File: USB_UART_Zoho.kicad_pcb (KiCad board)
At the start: 4 copper layers, 50 x 25 mm, 22 parts, among them J1 USB_C_Receptacle, J2 Peripherals, J4 VccIo_jumper, U1 FT232RL, U2 USBLC6-2P6

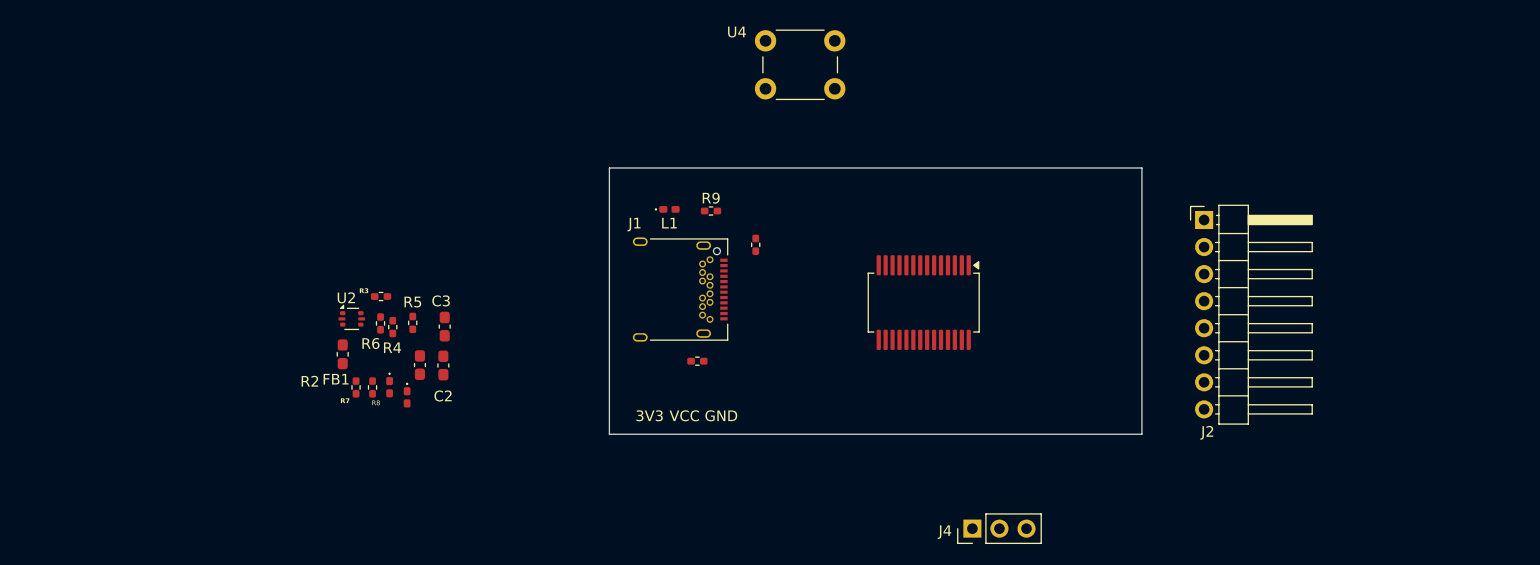
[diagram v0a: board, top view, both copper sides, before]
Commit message: USB type C changed to USB type A: some desgin changes in the routing
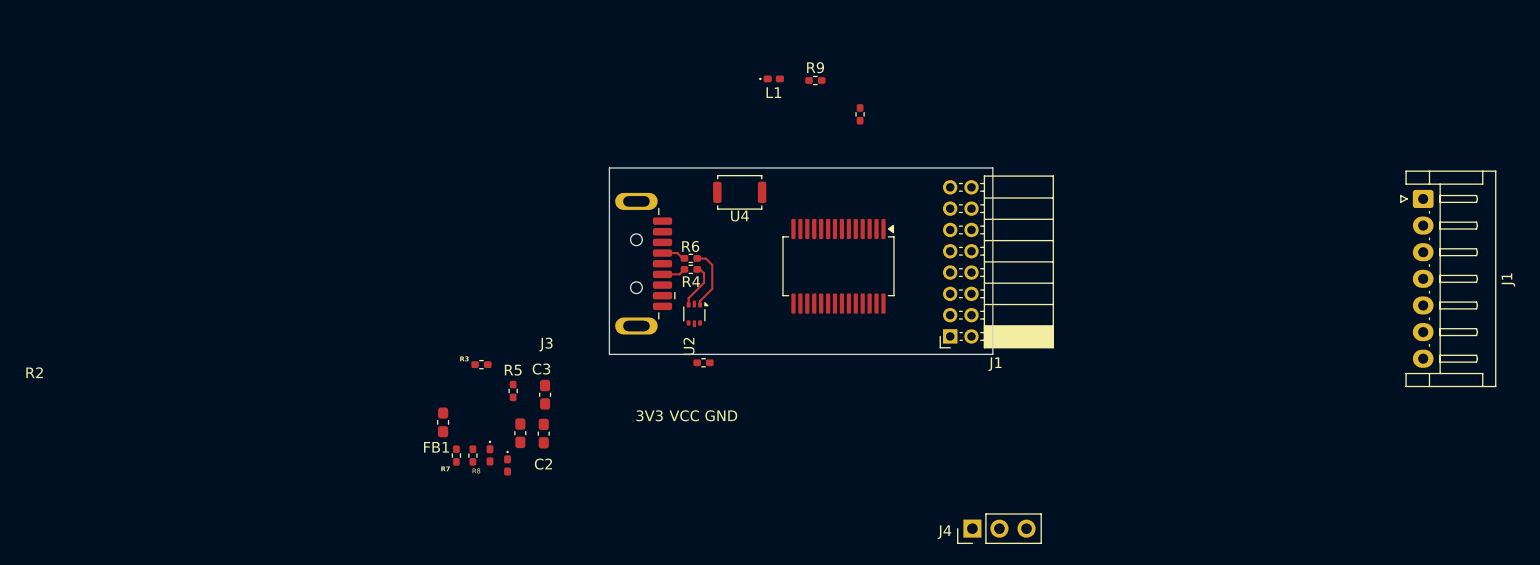
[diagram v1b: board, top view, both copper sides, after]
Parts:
- removed the J1 at (133.0, 95.0)
- removed J2: Peripherals, Connector_PinHeader_2.54mm:PinHeader_1x08_P2.54mm_Horizontal
- added J1: Conn_02x08_Counter_Clockwise, Connector_PinSocket_2.00mm:PinSocket_2x08_P2.00mm_Horizontal, F.Cu at (159.3, 99.4)
- added J1: Conn_01x07_Pin, Connector_JST:JST_EH_S7B-EH_1x07_P2.50mm_Horizontal, F.Cu at (203.7, 86.5)
- added J3: USB3_A, Connector_USB:USB3_A_Plug_Wuerth_692112030100_Horizontal, F.Cu at (121.4, 92.6)
- U4: footprint Button_Switch_THT:SW_PUSH_6mm_H5mm -> Button_Switch_SMD:SW_Push_SPST_NO_Alps_SKRK
- moved U2 32.2 mm to (135.2, 97.3), turned to -90 degrees
- moved R6 29.8 mm to (134.9, 92.1), turned to 180 degrees
- moved R4 28.5 mm to (134.9, 93.1), turned to 0 degrees
- moved R1 15.7 mm to (150.8, 78.6)
- moved L1 15.7 mm to (142.7, 75.2)
- moved R9 15.7 mm to (146.6, 75.4)
- moved U4 13.2 mm to (139.5, 85.9)
- moved C1 11.4 mm to (118.9, 108.5)
- moved FB1 11.4 mm to (111.7, 107.5)
- moved R7 11.4 mm to (112.9, 110.6)
- moved C3 11.4 mm to (121.2, 104.9)
- moved Rx_LED1 11.4 mm to (116.0, 110.6)
- moved Tx_LED1 11.4 mm to (117.7, 111.5)
- moved C2 11.4 mm to (121.1, 108.5)
- moved R3 11.4 mm to (115.2, 102.1)
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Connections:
- R6 pad 1: /D+ -> /d_P
- R6 pad 2: /d_P -> /D+
- U2 pad 1: /d_N -> /d_P
- U2 pad 3: /d_P -> /d_N
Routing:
- net /d_P: track 0.00 -> 5.88 mm
- net /d_N: track 0.00 -> 4.36 mm
- net /D+: track 0.00 -> 2.27 mm
- net /D-: track 0.00 -> 2.26 mm
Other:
- board size 50 x 25 mm -> 36 x 17.5 mm

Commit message: major rerouting done: decoupling capacitorsm and resistors placed
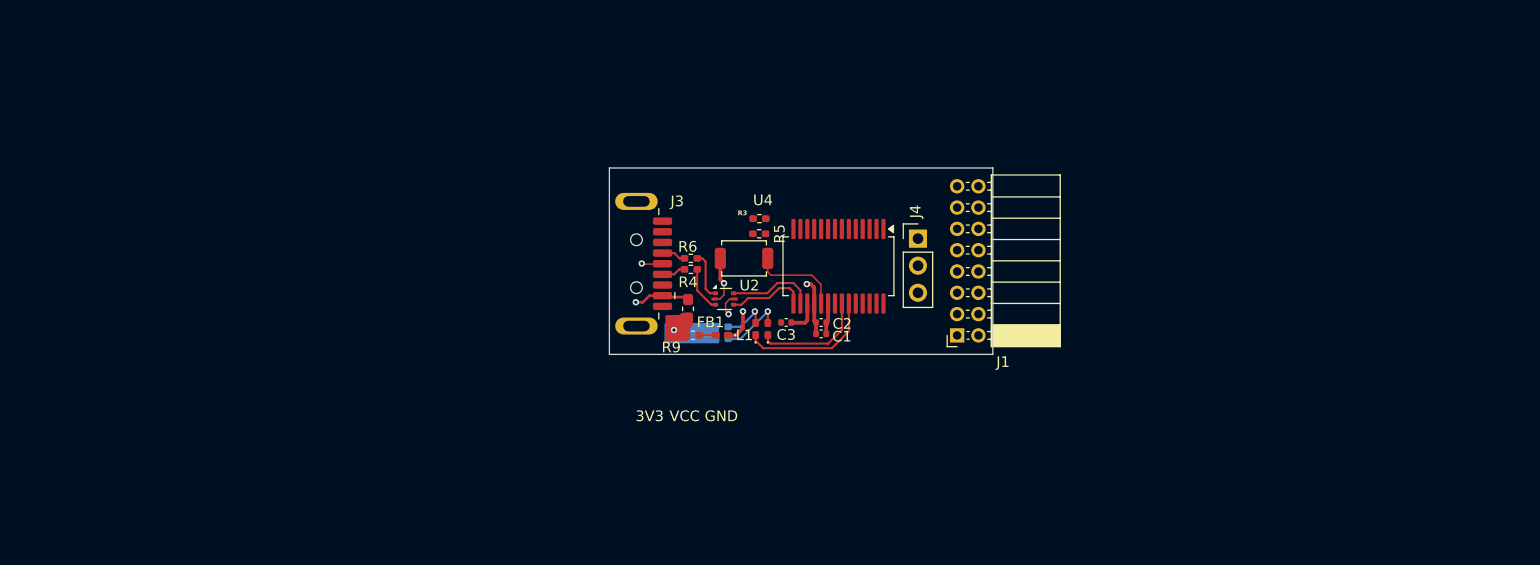
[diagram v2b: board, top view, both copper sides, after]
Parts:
- removed the J1 at (159.3, 99.4)
- removed the J1 at (203.7, 86.5)
- removed R1, R2: 5.1k, Resistor_SMD:R_0402_1005Metric_Pad0.72x0.64mm_HandSolder
- added J1: Conn_02x08_Counter_Clockwise, Connector_PinSocket_2.00mm:PinSocket_2x08_P2.00mm_Horizontal, F.Cu at (159.9, 99.3)
- C1, C2, C3: footprint Capacitor_SMD:C_0603_1608Metric_Pad1.08x0.95mm_HandSolder -> Capacitor_SMD:C_0402_1005Metric
- R7, R8: moved to B.Cu
- U4: footprint Button_Switch_SMD:SW_Push_SPST_NO_Alps_SKRK -> Button_Switch_SMD:SW_SPST_TS-1088-xR025
- moved C1 29.7 mm to (147.1, 99.2), turned to 180 degrees
- moved R3 29.5 mm to (141.4, 88.4)
- moved Rx_LED1 28.7 mm to (142.1, 98.7), turned to 90 degrees
- moved C2 28.1 mm to (147.1, 98.1), turned to 180 degrees
- moved J4 27.7 mm to (156.2, 90.2), turned to 0 degrees
- moved R7 27.7 mm to (137.8, 98.5), turned to 0 degrees
- moved R5 27.4 mm to (141.3, 89.8), turned to 0 degrees
- moved Tx_LED1 26.6 mm to (141.0, 98.7), turned to 90 degrees
- moved R9 26.5 mm to (135.1, 99.3), turned to 180 degrees
- moved R8 25.8 mm to (137.8, 99.6), turned to 0 degrees
- moved FB1 25.3 mm to (134.6, 96.8)
- moved L1 24.6 mm to (137.8, 99.3), turned to 180 degrees
- moved C3 23.6 mm to (143.9, 98.1), turned to 180 degrees
- moved U4 6.21 mm to (139.9, 92.1)
- moved U2 3.16 mm to (138.1, 95.9), turned to 0 degrees
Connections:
- FB1 pad 1: Net-(F1-Pad2) -> VBUS
- U1 pad 1: unconnected-(U1-TXD-Pad1) -> Net-(J1-Pin_1)
- U1 pad 10: unconnected-(U1-DCD-Pad10) -> Net-(J1-Pin_7)
- U1 pad 11: unconnected-(U1-CTS-Pad11) -> Net-(J1-Pin_4)
- U1 pad 2: unconnected-(U1-DTR-Pad2) -> Net-(J1-Pin_5)
- U1 pad 3: unconnected-(U1-RTS-Pad3) -> Net-(J1-Pin_3)
- U1 pad 5: unconnected-(U1-RXD-Pad5) -> Net-(J1-Pin_2)
- U1 pad 6: unconnected-(U1-RI-Pad6) -> Net-(J1-Pin_8)
- U1 pad 9: unconnected-(U1-DCR-Pad9) -> Net-(J1-Pin_6)
- U2 pad 1: /d_P -> /d_N
- U2 pad 3: /d_N -> /d_P
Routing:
- net GND: track 0.00 -> 15.0 mm, vias 0 -> 4
- net Net-(Tx_LED1-K): track 0.00 -> 12.8 mm
- net Net-(Rx_LED1-K): track 0.00 -> 10.6 mm
- net /RESET: track 0.00 -> 8.56 mm
- net /d-: track 0.00 -> 8.21 mm
- net /d+: track 0.00 -> 7.51 mm
- net VBUS: track 0.00 -> 7.43 mm, vias 0 -> 2
- net VCC: track 0.00 -> 7.08 mm, vias 0 -> 1
- net /Rx_LED: track 0.00 -> 5.85 mm, vias 0 -> 1
- net /Tx_LED: track 0.00 -> 4.22 mm, vias 0 -> 1
- net 3V3OUT: track 0.00 -> 3.18 mm
- net Net-(L1-A): track 0.00 -> 1.55 mm
- net /d_P: track 5.88 -> 4.58 mm
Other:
- board text removed: "OMKAR'S PCB"
- board text removed: "USB_UART_CONVERTER"

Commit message: routing complete: Rev 2/2 09/26
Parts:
- R7, R8: moved to F.Cu
- moved R8 4.67 mm to (138.5, 95.0)
- moved U2 3.38 mm to (138.1, 92.5)
- moved U4 3.33 mm to (138.0, 89.4)
- moved R7 2.36 mm to (138.5, 96.3)
- moved C3 1.79 mm to (145.6, 98.6), turned to -90 degrees
- moved R3 1.62 mm to (142.9, 88.7), turned to 90 degrees
- moved R5 1.11 mm to (141.7, 88.7), turned to 90 degrees
- moved R4 0.22 mm to (135.1, 93.1)
- moved R6 0.22 mm to (135.1, 92.1)
- moved J1 0.10 mm to (159.8, 99.4)
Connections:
- J1 pad 1: Net-(J1-Pin_1) -> unconnected-(J1-Pin_1-Pad1)
- J1 pad 10: unconnected-(J1-Pin_10-Pad10) -> unconnected-(U1-DTR-Pad2)
- J1 pad 2: Net-(J1-Pin_2) -> unconnected-(J1-Pin_2-Pad2)
- J1 pad 3: Net-(J1-Pin_3) -> unconnected-(J1-Pin_3-Pad3)
- J1 pad 4: Net-(J1-Pin_4) -> unconnected-(J1-Pin_4-Pad4)
- J1 pad 5: Net-(J1-Pin_5) -> unconnected-(J1-Pin_5-Pad5)
- J1 pad 6: Net-(J1-Pin_6) -> unconnected-(J1-Pin_6-Pad6)
- J1 pad 7: Net-(J1-Pin_7) -> unconnected-(J1-Pin_7-Pad7)
- J1 pad 8: Net-(J1-Pin_8) -> unconnected-(J1-Pin_8-Pad8)
- U1 pad 1: Net-(J1-Pin_1) -> unconnected-(J1-Pin_11-Pad11)
- U1 pad 10: Net-(J1-Pin_7) -> unconnected-(J1-Pin_15-Pad15)
- U1 pad 11: Net-(J1-Pin_4) -> unconnected-(J1-Pin_16-Pad16)
- U1 pad 2: Net-(J1-Pin_5) -> unconnected-(U1-DTR-Pad2)
- U1 pad 3: Net-(J1-Pin_3) -> unconnected-(J1-Pin_9-Pad9)
- U1 pad 5: Net-(J1-Pin_2) -> unconnected-(J1-Pin_12-Pad12)
- U1 pad 6: Net-(J1-Pin_8) -> unconnected-(J1-Pin_13-Pad13)
- U1 pad 9: Net-(J1-Pin_6) -> unconnected-(J1-Pin_14-Pad14)
- U2 pad 1: /d_N -> /d_P
- U2 pad 3: /d_P -> /d_N
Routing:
- net VCC: track 7.08 -> 29.5 mm, vias 1 -> 3
- net GND: track 15.0 -> 34.4 mm, vias 4 -> 5
- net unconnected-(J1-Pin_16-Pad16): track 0.00 -> 19.1 mm
- net unconnected-(J1-Pin_14-Pad14): track 0.00 -> 16.8 mm
- net unconnected-(J1-Pin_15-Pad15): track 0.00 -> 15.5 mm
- net unconnected-(J1-Pin_12-Pad12): track 0.00 -> 14.2 mm
- net 3V3OUT: track 3.18 -> 17.1 mm, vias 0 -> 1
- net unconnected-(U1-DTR-Pad2): track 0.00 -> 12.8 mm
- net unconnected-(J1-Pin_13-Pad13): track 0.00 -> 12.4 mm
- net unconnected-(J1-Pin_9-Pad9): track 0.00 -> 10.0 mm
- net unconnected-(J1-Pin_11-Pad11): track 0.00 -> 8.02 mm
- net VCCIO: track 0.00 -> 7.80 mm
- net /RESET: track 8.56 -> 14.5 mm
- net /d_P: track 4.58 -> 1.57 mm
- net Net-(U1-CBUS3): track 0.00 -> 2.85 mm
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- added copper zone on B.Cu, net GND
- added copper zone on B.Cu, net VCC
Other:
- board text added: "USB2 to UART Rev 2/2 09/26"
